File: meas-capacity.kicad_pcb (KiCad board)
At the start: 2 copper layers, 100 x 100 mm, 22 parts, among them J2 Probe1, J3 Probe2, J4 Probe3, J5 Probe4, J6 CAN1, J7 CAN2, P1 CONN_PROG+SER_AVR, Q1 BSS138, U1 ATMEGA168PA-AU, U2 MCP2515-E/SO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

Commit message: Add 5V regulator to capacity measurement module
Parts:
- added C7: 2.2u, Capacitor_SMD:C_0805_2012Metric, B.Cu at (255.5, 124.0)
- added U4: LP2950-5.0_TO92, Package_TO_SOT_THT:TO-92, F.Cu at (252.5, 125.5)
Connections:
- J6 pad 2: VCC -> Net-(J6-Pad2)
- J7 pad 2: VCC -> Net-(J6-Pad2)
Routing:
- net VCC: track 156.5 -> 128.4 mm
- net Net-(J6-Pad2): track 0.00 -> 27.4 mm
- net GNDD: track 156.2 -> 165.4 mm

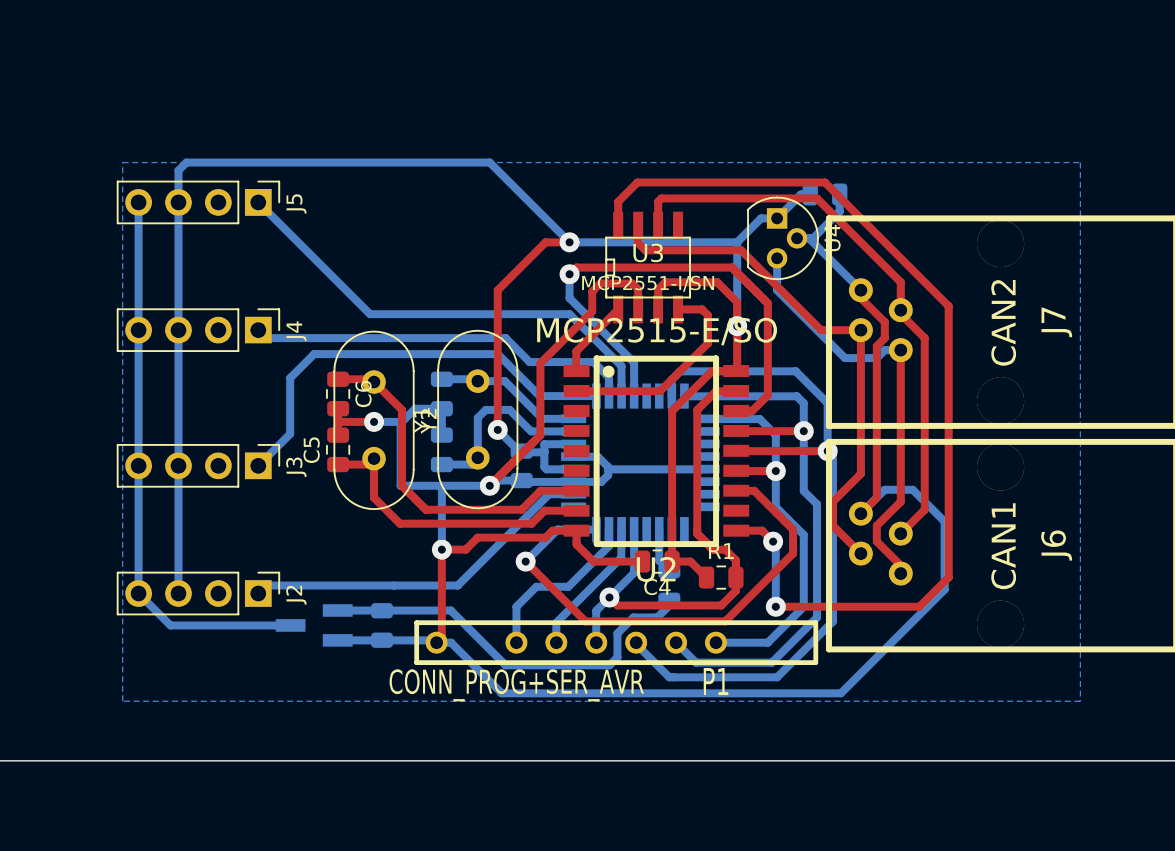
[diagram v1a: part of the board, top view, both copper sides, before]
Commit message: Use Mini-DIN plug
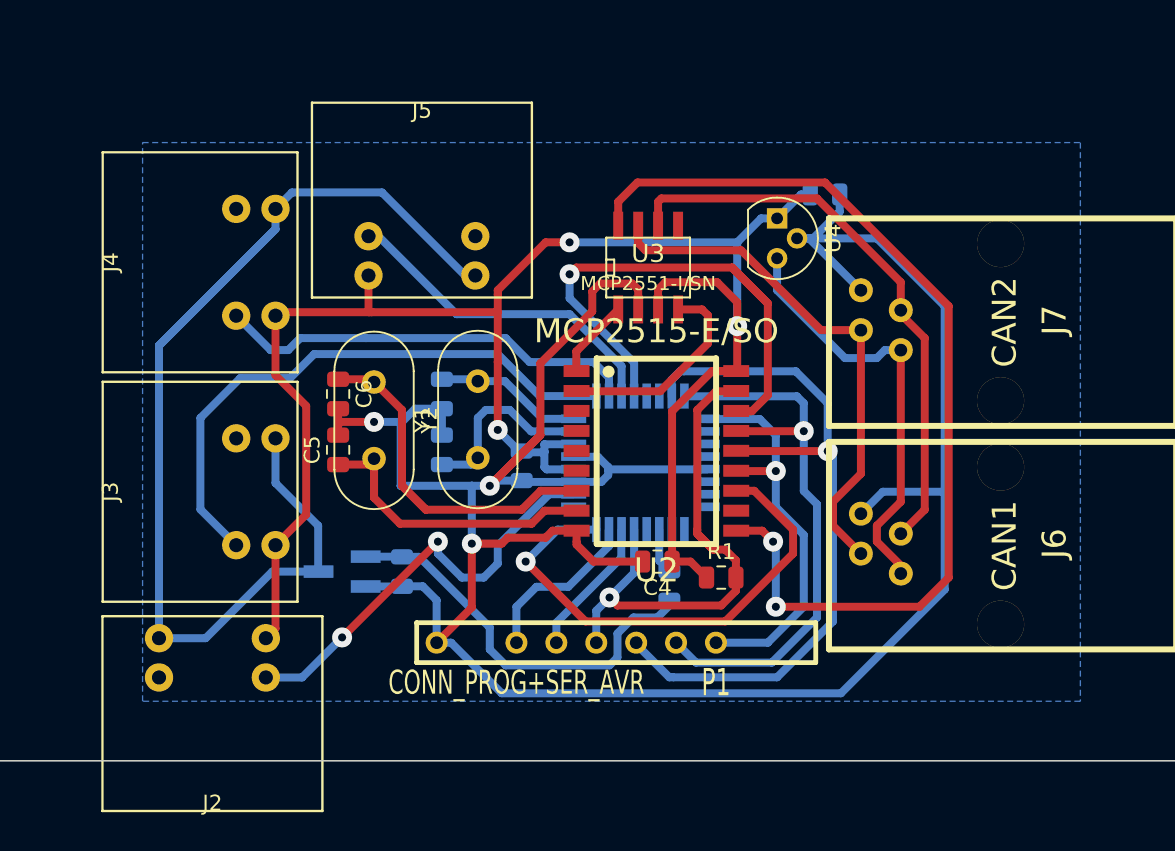
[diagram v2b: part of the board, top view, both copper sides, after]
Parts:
- C7: value 2.2u -> 4.7u
- J2, J3, J4, J5: footprint Connector_PinHeader_2.54mm:PinHeader_1x04_P2.54mm_Vertical -> Connectors_K:CONN_MINI_DIN_4
- moved J2 14.1 mm to (216.5, 163.2), turned to 180 degrees
- moved J5 12.2 mm to (229.9, 118.1), turned to 0 degrees
- moved J4 10.8 mm to (209.6, 128.3), turned to 90 degrees
- moved J3 10.0 mm to (209.6, 142.9), turned to 90 degrees
- moved Q1 3.86 mm to (224.8, 148.0)
- moved R3 3.66 mm to (228.6, 148.0)
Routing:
- net Net-(J2-Pad4): track 35.4 -> 95.7 mm
- net VCC: track 128.4 -> 113.5 mm
- net Net-(J3-Pad1): track 27.7 -> 37.0 mm
- net GNDD: track 165.4 -> 173.8 mm
- net Net-(J5-Pad1): track 29.3 -> 21.7 mm
- net Net-(J2-Pad1): track 22.7 -> 27.4 mm, vias 0 -> 2
- net Net-(J4-Pad1): track 24.7 -> 27.2 mm
- net Net-(Q1-Pad1): track 25.1 -> 25.8 mm

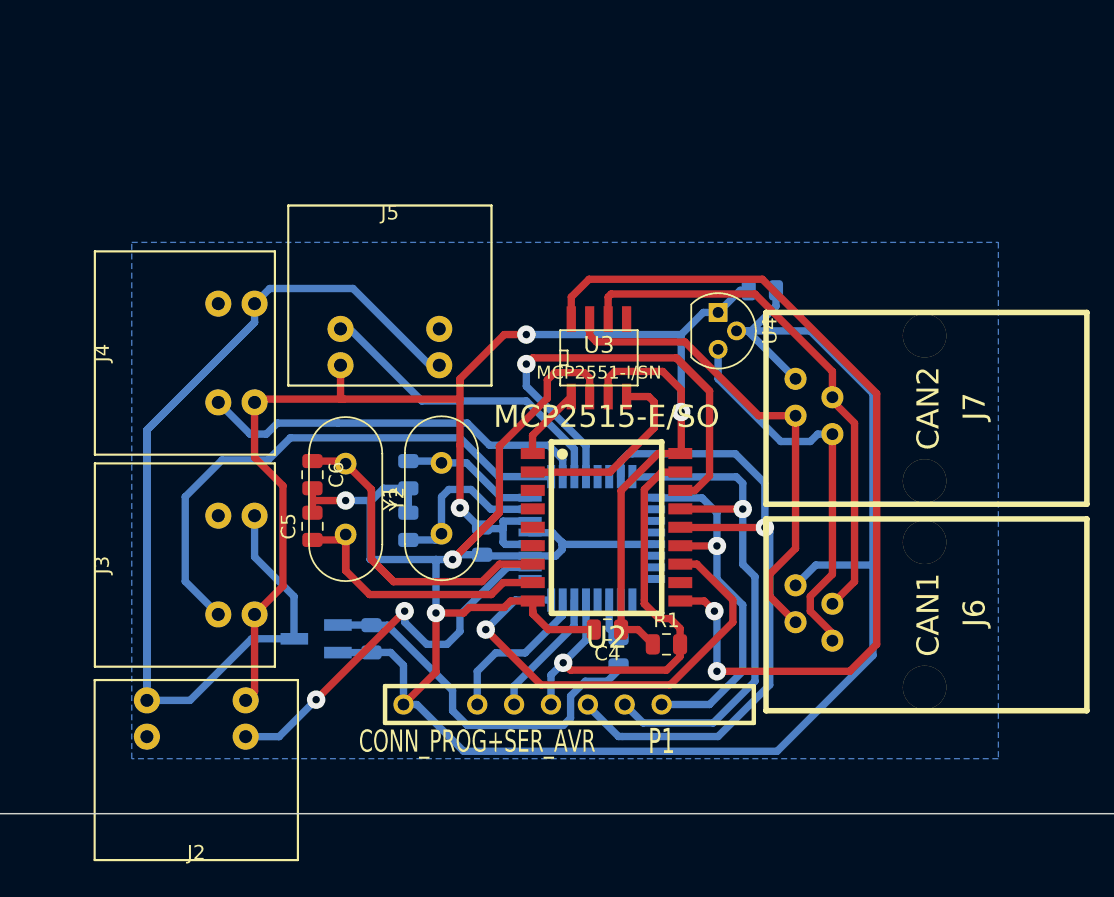
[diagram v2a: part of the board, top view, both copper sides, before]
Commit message: Move all plugs onto one side of the PCB
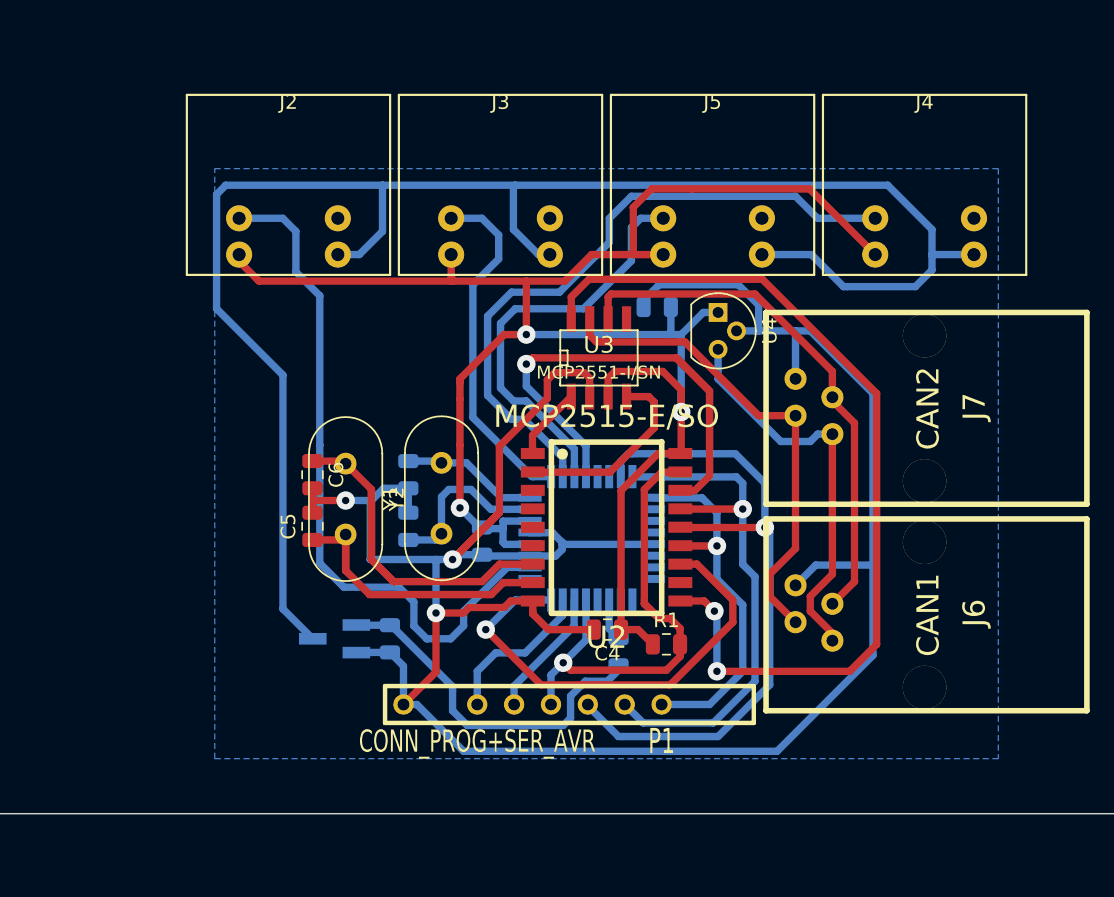
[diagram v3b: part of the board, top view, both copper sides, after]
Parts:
- moved J4 59.9 mm to (266.7, 110.5), turned to 0 degrees
- moved J2 53.1 mm to (222.9, 110.5), turned to 0 degrees
- moved J3 42.8 mm to (237.5, 110.5), turned to 0 degrees
- moved J5 23.5 mm to (252.1, 110.5)
- moved C7 7.33 mm to (248.3, 125.1), turned to 180 degrees
- moved Q1 1.27 mm to (226.1, 148.0)
- moved R3 1.27 mm to (229.9, 148.0)
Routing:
- net Net-(J2-Pad1): track 27.4 -> 48.1 mm, vias 2 -> 0
- net Net-(J2-Pad4): track 95.7 -> 116.2 mm
- net VCC: track 113.5 -> 132.9 mm
- net Net-(J4-Pad1): track 27.2 -> 45.4 mm
- net Net-(J3-Pad1): track 37.0 -> 24.1 mm
- net Net-(J5-Pad1): track 21.7 -> 28.7 mm
- net GNDD: track 173.8 -> 178.3 mm
- net Net-(Q1-Pad1): track 25.8 -> 24.7 mm

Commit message: Adjust edge, add text
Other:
- board size 100 x 100 mm -> 57.8 x 44.4 mm
- board text added: "2018 KSZ"
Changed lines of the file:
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@@
   (general
     (thickness 1.6)
-    (drawings 4)
+    (drawings 6)
     (tracks 384)
     (zones 0)
@@
   )
   (page A4)
+  (title_block
+    (title "Capacitive soil water content measurement board")
+    (company "Klaus Schneider-Zapp")
+  )
   (layers
     (0 F.Cu signal)
@@
     )
   )
-  (gr_line (start 180 60) (end 180 160) (angle 90) (layer Edge.Cuts) (width 0.1))
-  (gr_line (start 280 60) (end 180 60) (angle 90) (layer Edge.Cuts) (width 0.1))
-  (gr_line (start 280 160) (end 280 60) (angle 90) (layer Edge.Cuts) (width 0.1))
-  (gr_line (start 180 160) (end 280 160) (angle 90) (layer Edge.Cuts) (width 0.1))
+  (gr_text "2018 KSZ" (at 223.52 154.94) (layer F.Cu)
+    (effects (font (size 1.5 1.5) (thickness 0.3)))
+  )
+  (gr_text "2018 KSZ" (at 223.52 154.94) (layer B.Cu)
+    (effects (font (size 1.5 1.5) (thickness 0.3)) (justify mirror))
+  )
+  (gr_line (start 216.535 157.48) (end 216.535 113.03) (angle 90) (layer Edge.Cuts) (width 0.1))
+  (gr_line (start 274.32 157.48) (end 216.535 157.48) (angle 90) (layer Edge.Cuts) (width 0.1))
+  (gr_line (start 274.32 113.03) (end 274.32 157.48) (angle 90) (layer Edge.Cuts) (width 0.1))
+  (gr_line (start 216.535 113.03) (end 274.32 113.03) (angle 90) (layer Edge.Cuts) (width 0.1))
   (segment (start 231.14 141.1455) (end 232.9965 141.1455) (width 0.508) (layer B.Cu) (net 1) (status C00000))
   (segment (start 232.9965 141.1455) (end 233.426 140.716) (width 0.508) (layer B.Cu) (net 1) (status C00000))
